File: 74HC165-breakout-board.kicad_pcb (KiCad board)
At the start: 2 copper layers, 88 x 40 mm, 34 parts, among them J1 Conn_01x05, J10 Conn_01x04, J2 Conn_01x05, J3 Conn_01x05, J4 Conn_01x05, J5 Conn_01x05, J6 Conn_01x05, J7 Conn_01x05, J8 Conn_01x05, J9 Conn_01x05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

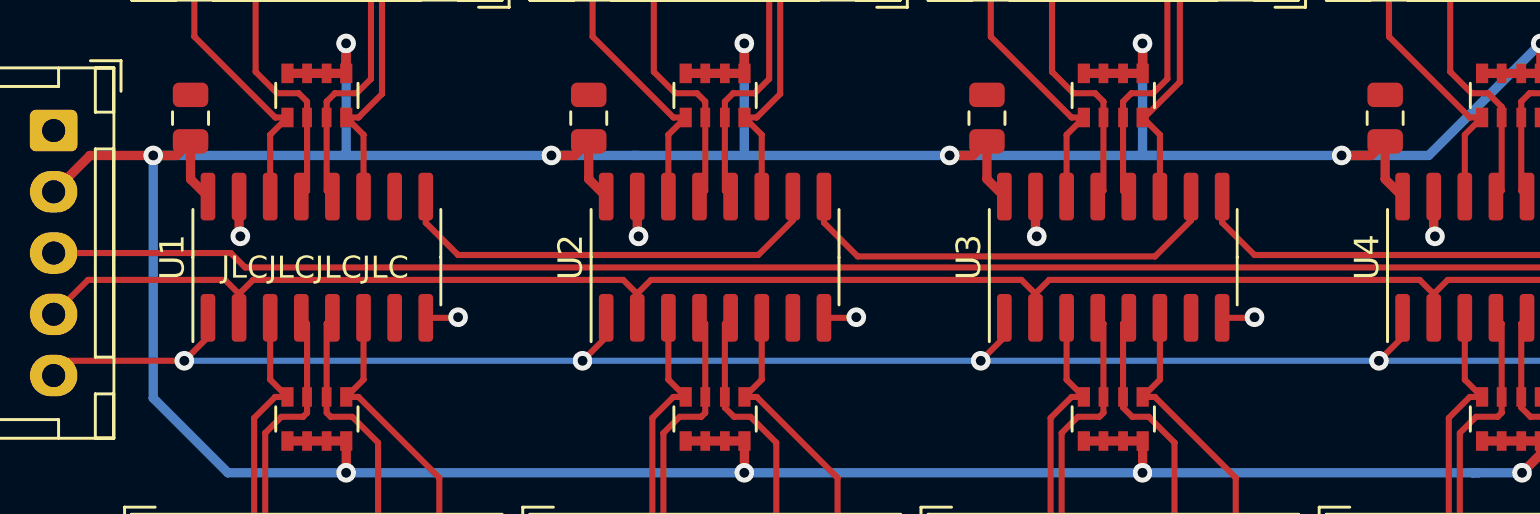
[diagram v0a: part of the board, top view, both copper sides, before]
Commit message: Add pin numbers to back of board Fixes #3
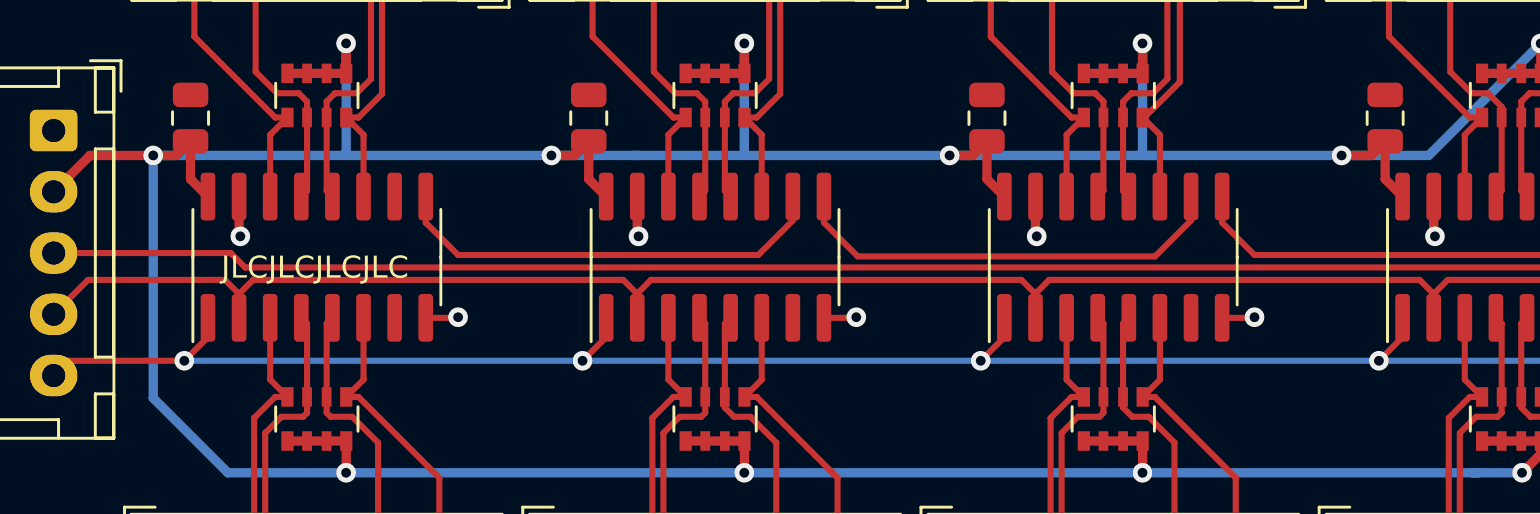
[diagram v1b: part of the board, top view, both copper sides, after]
